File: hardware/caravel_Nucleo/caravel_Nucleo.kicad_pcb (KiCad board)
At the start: 4 copper layers, 68.1 x 92.5 mm, 106 parts, among them IC1 74LVC2G32DP,125, J1 USB4105-GF-A, J10 PinHeader_1x11, J11 PinHeader_1x02, J12 PinHeader_1x02, J13 PinHeader_1x02, J2 PinHeader_1x02, J3 PinHeader_1x02, J4 61300411121, J5 PinHeader_1x02, J6 PinHeader_1x02, J7 61300611121, J8 640456-3, J9 640456-3, Q1 BSS84AKW, SW1 KMR2, T1 Logo, T2 Logo, U1 FT232HQ, U12 NUCLEO144-F429ZI, U2 SN74LVC1G125DCKR, U3 SN74LVC1G125DCKR, U4 MAX811REUS+T, U5 MCP4661-103E/ML, U6 Caravel_breakout_PCB, U7 W25Q32FVSS, U8 NTS0102DP, U9 MIC2211-AAYML-TR, X1 ECS-2520MVLC-100-BN-TR, Y1 ABM8G-12.000MHZ-18-D2Y-T

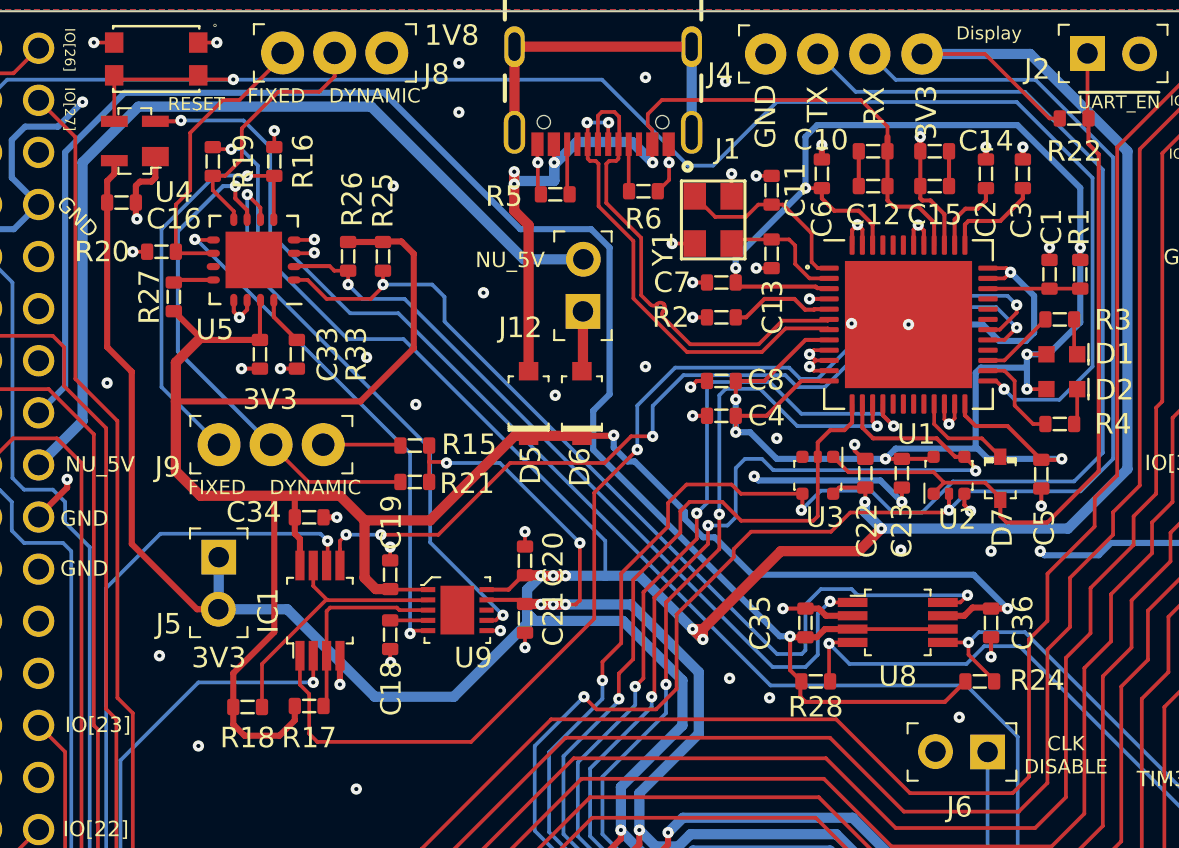
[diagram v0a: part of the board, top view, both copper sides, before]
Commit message: Optimize GND via placment
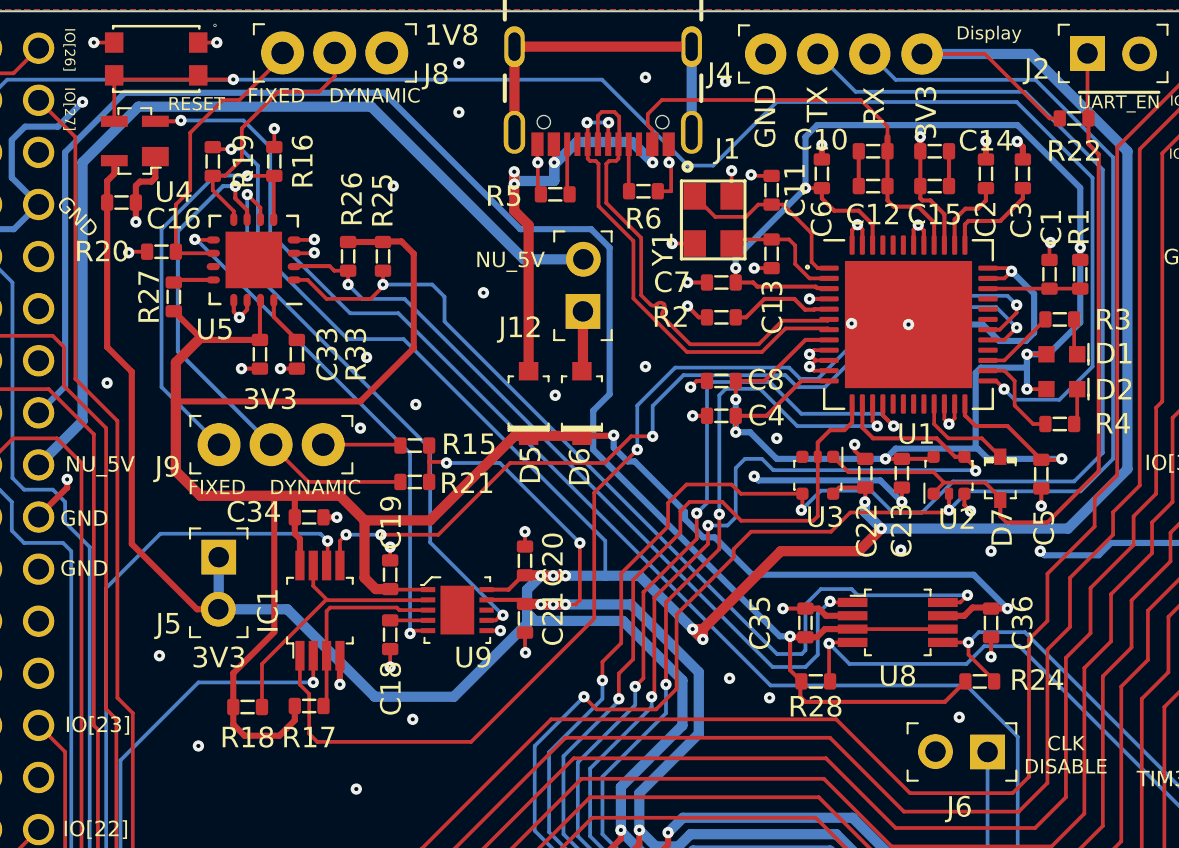
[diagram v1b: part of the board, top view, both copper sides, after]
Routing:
- net AGND: track 224.2 -> 228.0 mm, vias 112 -> 114

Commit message: Update PCB with new components
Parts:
- C1, C10, C11, C12, C13, C14, C15, C16, C17, C18, C19, C2, C20, C21, C22, C23, C24, C25, C26, C27, C28, C29, C3, C30, C31, C32, C33, C34, C35, C36, C4, C5, C6, C7, C8, C9: footprint antmicro-footprints:0603-cap -> caravel_Nucleo-footprints:0603-cap
- D1, D2, D3, D4: footprint antmicro-footprints:LED_0603 -> caravel_Nucleo-footprints:LED_0603
- D5, D6: footprint antmicro-footprints:SOD-123 -> caravel_Nucleo-footprints:SOD-123
- D7: footprint antmicro-footprints:SOD-323F -> caravel_Nucleo-footprints:SOD-323F
- IC1, U8: footprint antmicro-footprints:TSSOP-8_W3mm -> caravel_Nucleo-footprints:TSSOP-8_W3mm
- J1: footprint antmicro-footprints:GCT_USB4105-GF-A -> caravel_Nucleo-footprints:GCT_USB4105-GF-A
- J10: footprint antmicro-footprints:PinHeader_1x11_P2.54_Vertical -> caravel_Nucleo-footprints:PinHeader_1x11_P2.54_Vertical
- J11, J12, J13, J2, J3, J5, J6: footprint antmicro-footprints:PinHeader_1x2_P2.54mm -> caravel_Nucleo-footprints:PinHeader_1x2_P2.54mm
- J4: footprint antmicro-footprints:PinHeader_1x4_P2.54mm_Drill1.02mm -> caravel_Nucleo-footprints:PinHeader_1x4_P2.54mm_Drill1.02mm
- J7: footprint antmicro-footprints:61300611121 -> caravel_Nucleo-footprints:61300611121
- J8, J9: footprint antmicro-footprints:PinHeader_1x3_P2.54_Drill1.1mm -> caravel_Nucleo-footprints:PinHeader_1x3_P2.54_Drill1.1mm
- Q1: footprint antmicro-footprints:SOT-323 -> caravel_Nucleo-footprints:SOT-323
- R1, R10, R11, R12, R13, R14, R15, R16, R17, R18, R19, R2, R20, R21, R22, R23, R24, R25, R26, R27, R28, R29, R3, R30, R31, R32, R33, R4, R5, R6, R7, R8, R9: footprint antmicro-footprints:0603-res -> caravel_Nucleo-footprints:0603-res
- SW1: footprint antmicro-footprints:SW_SPST_4.2x2.8 -> caravel_Nucleo-footprints:SW_SPST_4.2x2.8
- T1: value Logo -> efabless_logo; footprint antmicro-footprints:efabless_logo_2 -> caravel_Nucleo-footprints:efabless_logo
- T2: value Logo -> efabless_logo; footprint antmicro-footprints:efabless_logo -> caravel_Nucleo-footprints:efabless_logo
- U1: footprint antmicro-footprints:QFN-48-1EP_8x8mm_P0.5mm_EP6.2x6.2mm_FT232HQ_marking -> caravel_Nucleo-footprints:QFN-48-1EP_8x8mm_P0.5mm_EP6.2x6.2mm_FT232HQ_marking
- U12: footprint antmicro-footprints:ST_Morpho_Connectors_144 -> caravel_Nucleo-footprints:ST_Morpho_Connectors_144
- U2, U3: footprint antmicro-footprints:SOT-353 -> caravel_Nucleo-footprints:SOT-353
- U4: footprint antmicro-footprints:SOT-143-4 -> caravel_Nucleo-footprints:SOT-143-4
- U5: footprint antmicro-footprints:QFN-16_EP_4x4_Pitch0.65mm -> caravel_Nucleo-footprints:QFN-16_EP_4x4_Pitch0.65mm
- U6: footprint antmicro-footprints:caravel_breakout -> caravel_Nucleo-footprints:caravel_breakout
- U7: footprint antmicro-footprints:SOIC127P790X216-8N -> caravel_Nucleo-footprints:SOIC127P790X216-8N
- U9: footprint antmicro-footprints:DFN-10-1EP_3x3mm -> caravel_Nucleo-footprints:DFN-10-1EP_3x3mm
- X1: footprint antmicro-footprints:Oscillator_SMD_ECS_2520MV-xxx-xx-4Pin_2.5x2.0mm -> caravel_Nucleo-footprints:Oscillator_SMD_ECS_2520MV-xxx-xx-4Pin_2.5x2.0mm
- Y1: footprint antmicro-footprints:KX-7 -> caravel_Nucleo-footprints:KX-7
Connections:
- U9 pad 11: (no net) -> AGND

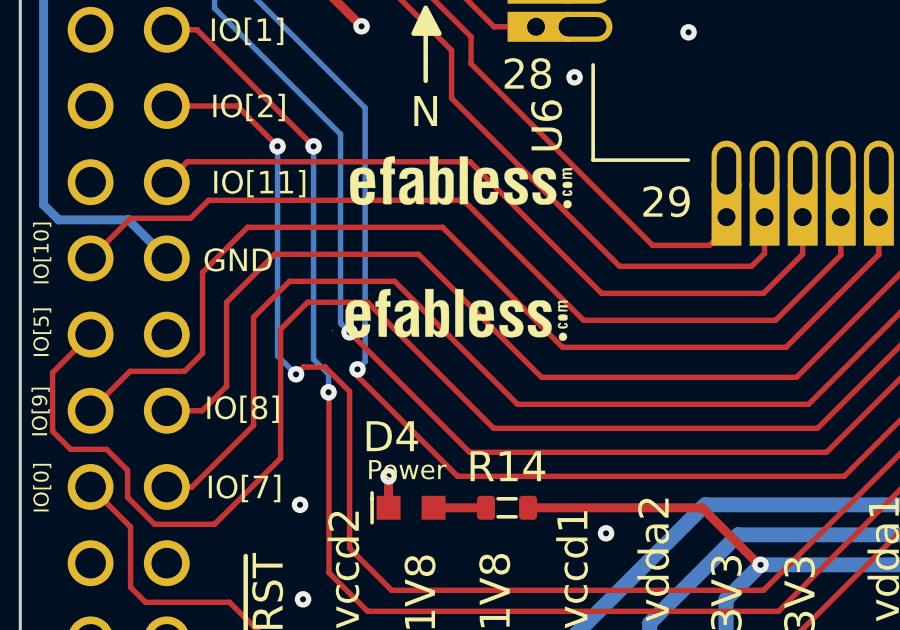
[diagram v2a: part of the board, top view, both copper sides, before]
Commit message: Update Efabless logo on PCB
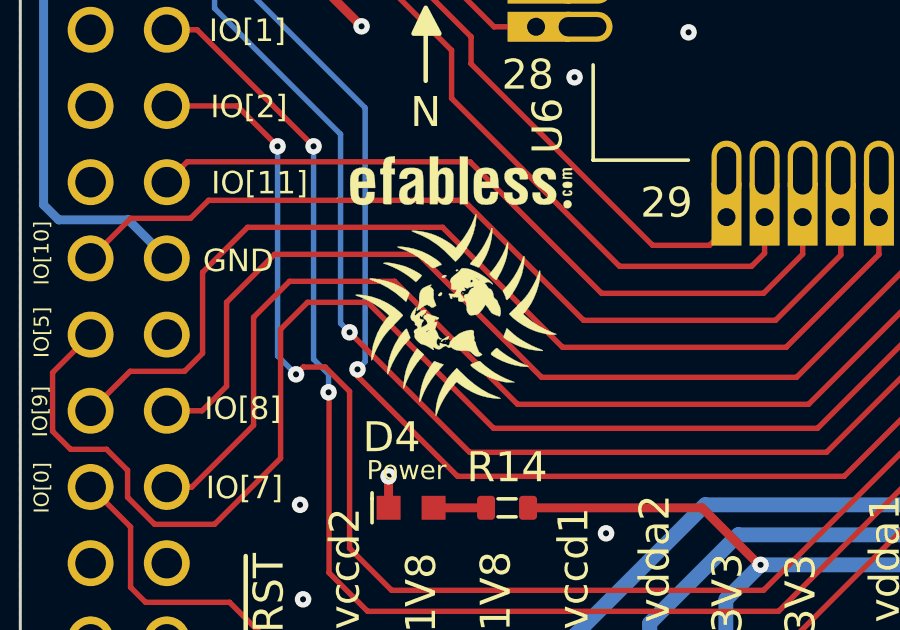
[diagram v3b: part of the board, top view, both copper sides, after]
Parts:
- T1: footprint caravel_Nucleo-footprints:efabless_logo -> caravel_Nucleo-footprints:logo
